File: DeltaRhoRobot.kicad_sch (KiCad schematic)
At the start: 37 parts, among them J1 Conn_01x02_Socket, J2 USB_C_Receptacle_USB2.0, J3 USB_C_Receptacle_USB2.0, Q1 MBT3904DW1, Q3 STB55NF06T4, SW1 CAS-120A1, U1 AP63205WU-7, U2 AMS1117-3.3

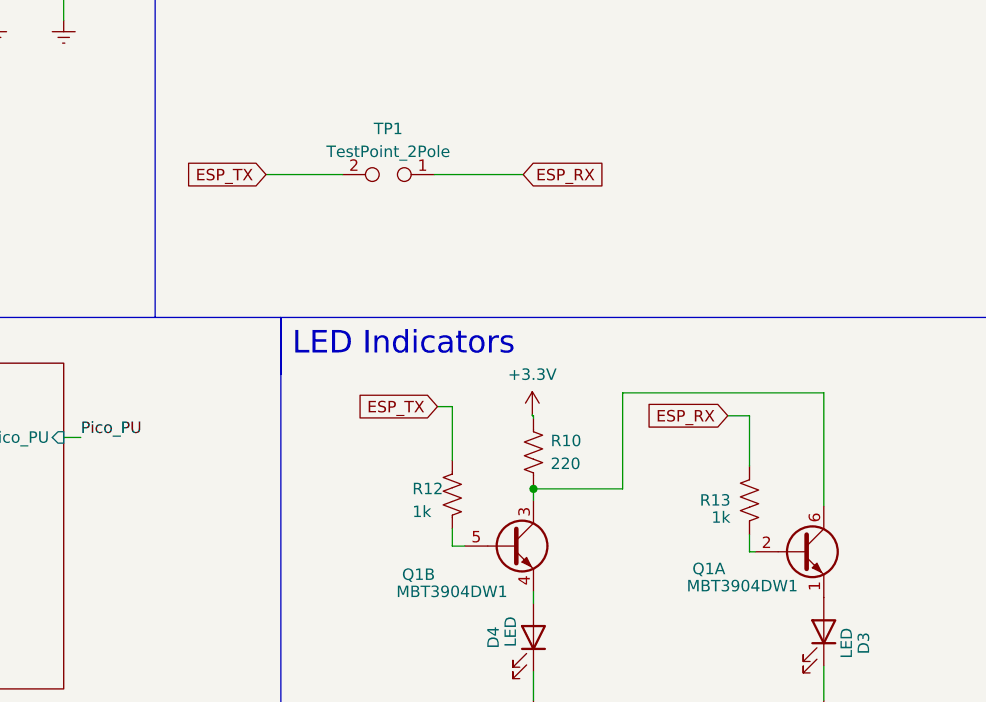
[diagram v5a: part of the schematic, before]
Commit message: update to I2C
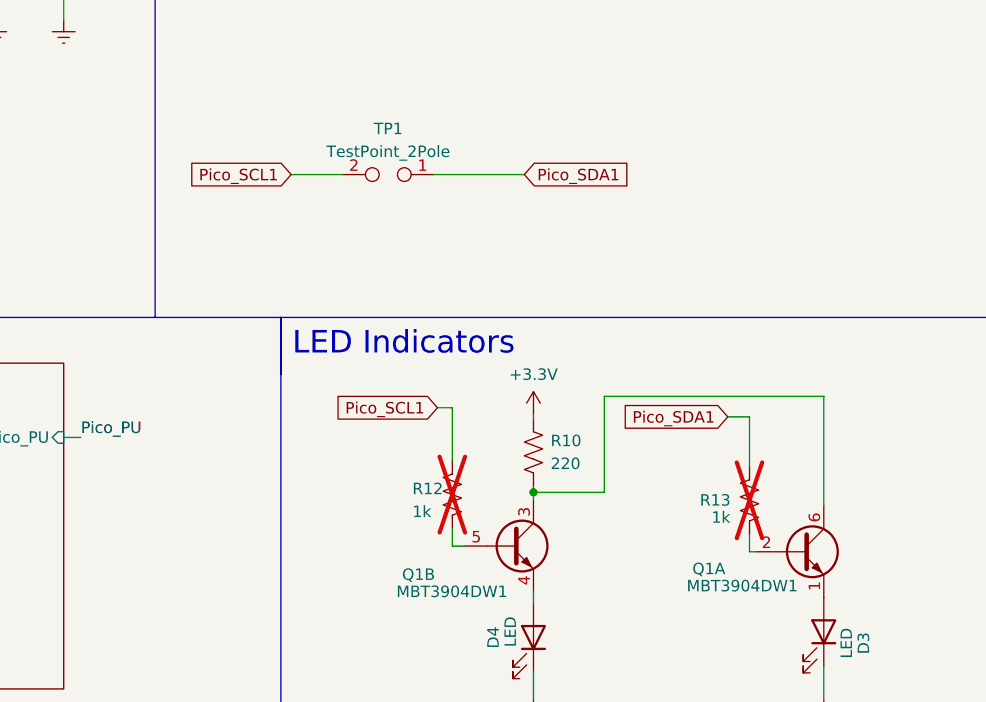
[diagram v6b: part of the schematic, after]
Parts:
- R12, R13: footprint Resistor_SMD:R_0402_1005Metric -> Resistor_SMD:R_1210_3225Metric_Pad1.30x2.65mm_HandSolder; now not fitted
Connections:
- net ESP_RX renamed Pico_SDA1
- net ESP_TX renamed Pico_SCL1
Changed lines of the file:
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@@
 (kicad_sch (version 20230121) (generator eeschema)
   (paper "A4")
+  (junction (at 124.968 170.434) (diameter 0) (color 0 0 0 0)
+  )
   (junction (at 261.366 41.783) (diameter 0) (color 0 0 0 0)
   )
@@
   )
   (junction (at 46.736 107.823) (diameter 0) (color 0 0 0 0)
-  )
-  (junction (at 124.968 170.053) (diameter 0) (color 0 0 0 0)
   )
   (no_connect (at 93.853 109.347))
@@
     (stroke (width 0) (type default))
   )
-  (wire (pts (xy 115.951 160.909) (xy 115.951 166.878))
+  (wire (pts (xy 115.951 161.036) (xy 115.951 166.878))
     (stroke (width 0) (type default))
   )
@@
     (stroke (width 0) (type default))
   )
-  (wire (pts (xy 124.841 161.925) (xy 124.841 161.798))
-    (stroke (width 0) (type default))
-  )
   (wire (pts (xy 54.991 112.903) (xy 46.736 112.903))
     (stroke (width 0) (type default))
@@
     (stroke (width 0) (type default))
   )
+  (wire (pts (xy 124.968 170.434) (xy 124.968 171.323))
+    (stroke (width 0) (type default))
+  )
   (wire (pts (xy 125.984 53.975) (xy 125.984 60.833))
     (stroke (width 0) (type default))
@@
     (stroke (width 0) (type default))
   )
+  (wire (pts (xy 124.968 169.799) (xy 124.968 170.434))
+    (stroke (width 0) (type default))
+  )
   (wire (pts (xy 236.601 51.308) (xy 254.381 51.308))
     (stroke (width 0) (type default))
@@
     (stroke (width 0) (type default))
   )
-  (wire (pts (xy 146.558 161.925) (xy 148.971 161.925))
+  (wire (pts (xy 146.558 162.052) (xy 148.971 162.052))
     (stroke (width 0) (type default))
   )
@@
     (stroke (width 0) (type default))
   )
-  (wire (pts (xy 124.968 161.925) (xy 124.841 161.925))
-    (stroke (width 0) (type default))
-  )
   (wire (pts (xy 64.516 43.053) (xy 64.516 46.228))
     (stroke (width 0) (type default))
@@
     (stroke (width 0) (type default))
   )
-  (wire (pts (xy 95.25 135.128) (xy 103.759 135.128))
+  (wire (pts (xy 98.044 135.128) (xy 103.759 135.128))
     (stroke (width 0) (type default))
   )
@@
     (stroke (width 0) (type default))
   )
-  (wire (pts (xy 124.968 169.799) (xy 124.968 170.053))
-    (stroke (width 0) (type default))
-  )
   (wire (pts (xy 48.006 39.878) (xy 58.166 39.878))
     (stroke (width 0) (type default))
@@
     (stroke (width 0) (type default))
   )
-  (wire (pts (xy 124.968 161.925) (xy 124.968 162.179))
+  (wire (pts (xy 124.968 161.798) (xy 124.968 162.179))
     (stroke (width 0) (type default))
   )
@@
     (stroke (width 0) (type default))
   )
-  (wire (pts (xy 148.971 161.925) (xy 148.971 167.513))
-    (stroke (width 0) (type default))
-  )
-  (wire (pts (xy 124.968 170.053) (xy 134.874 170.053))
+  (wire (pts (xy 148.971 162.052) (xy 148.971 167.513))
+    (stroke (width 0) (type default))
+  )
+  (wire (pts (xy 124.968 170.434) (xy 132.842 170.434))
     (stroke (width 0) (type default))
   )
@@
     (stroke (width 0) (type default))
   )
-  (wire (pts (xy 134.874 159.385) (xy 157.226 159.385))
+  (wire (pts (xy 132.842 159.766) (xy 157.226 159.766))
     (stroke (width 0) (type default))
   )
@@
     (stroke (width 0) (type default))
   )
-  (wire (pts (xy 134.874 170.053) (xy 134.874 159.385))
+  (wire (pts (xy 132.842 170.434) (xy 132.842 159.766))
     (stroke (width 0) (type default))
   )
@@
     (stroke (width 0) (type default))
   )
-  (wire (pts (xy 124.968 170.053) (xy 124.968 171.323))
-    (stroke (width 0) (type default))
-  )
-  (wire (pts (xy 114.3 160.909) (xy 115.951 160.909))
-    (stroke (width 0) (type default))
-  )
-  (wire (pts (xy 157.226 159.385) (xy 157.226 171.958))
+  (wire (pts (xy 114.3 161.036) (xy 115.951 161.036))
+    (stroke (width 0) (type default))
+  )
+  (wire (pts (xy 157.226 159.766) (xy 157.226 171.958))
     (stroke (width 0) (type default))
   )
@@
     (stroke (width 0) (type default))
   )
-  (wire (pts (xy 123.825 135.128) (xy 113.919 135.128))
+  (wire (pts (xy 113.919 135.128) (xy 123.952 135.128))
     (stroke (width 0) (type default))
   )
@@
     (effects (font (size 1.27 1.27)) (justify left bottom))
   )
-  (global_label "ESP_RX" (shape input) (at 146.558 161.925 180) (fields_autoplaced)
+  (global_label "Pico_SCL1" (shape input) (at 98.044 135.128 180) (fields_autoplaced)
     (effects (font (size 1.27 1.27)) (justify right))
-    (property "Intersheetrefs" "${INTERSHEET_REFS}" (at 136.4972 161.925 0)
+    (property "Intersheetrefs" "${INTERSHEET_REFS}" (at 85.2617 135.128 0)
       (effects (font (size 1.27 1.27)) (justify right) hide)
     )
   )
-  (global_label "ESP_TX" (shape input) (at 114.3 160.909 180) (fields_autoplaced)
+  (global_label "Pico_SDA1" (shape input) (at 123.952 135.128 0) (fields_autoplaced)
+    (effects (font (size 1.27 1.27)) (justify left))
+    (property "Intersheetrefs" "${INTERSHEET_REFS}" (at 136.7948 135.128 0)
+      (effects (font (size 1.27 1.27)) (justify left) hide)
+    )
+  )
+  (global_label "Pico_SCL1" (shape input) (at 114.3 161.036 180) (fields_autoplaced)
     (effects (font (size 1.27 1.27)) (justify right))
-    (property "Intersheetrefs" "${INTERSHEET_REFS}" (at 104.5416 160.909 0)
+    (property "Intersheetrefs" "${INTERSHEET_REFS}" (at 101.5177 161.036 0)
       (effects (font (size 1.27 1.27)) (justify right) hide)
     )
   )
-  (global_label "ESP_RX" (shape input) (at 123.825 135.128 0) (fields_autoplaced)
-    (effects (font (size 1.27 1.27)) (justify left))
-    (property "Intersheetrefs" "${INTERSHEET_REFS}" (at 133.8858 135.128 0)
-      (effects (font (size 1.27 1.27)) (justify left) hide)
-    )
-  )
-  (global_label "ESP_TX" (shape input) (at 95.25 135.128 180) (fields_autoplaced)
+  (global_label "Pico_SDA1" (shape input) (at 146.558 162.052 180) (fields_autoplaced)
     (effects (font (size 1.27 1.27)) (justify right))
-    (property "Intersheetrefs" "${INTERSHEET_REFS}" (at 85.4916 135.128 0)
+    (property "Intersheetrefs" "${INTERSHEET_REFS}" (at 133.7152 162.052 0)
       (effects (font (size 1.27 1.27)) (justify right) hide)
     )
@@
     )
   )
-  (symbol (lib_id "power:+3.3V") (at 124.841 161.798 0) (mirror y) (unit 1)
-    (in_bom yes) (on_board yes) (dnp no) (fields_autoplaced)
-    (property "Reference" "#PWR022" (at 124.841 165.608 0)
-      (effects (font (size 1.27 1.27)) hide)
-    )
-    (property "Value" "+3.3V" (at 124.841 157.353 0)
-      (effects (font (size 1.27 1.27)))
-    )
-    (property "Footprint" "" (at 124.841 161.798 0)
-      (effects (font (size 1.27 1.27)) hide)
-    )
-    (property "Datasheet" "" (at 124.841 161.798 0)
+  (symbol (lib_id "power:+3.3V") (at 124.968 161.798 0) (mirror y) (unit 1)
+    (in_bom yes) (on_board yes) (dnp no) (fields_autoplaced)
+    (property "Reference" "#PWR022" (at 124.968 165.608 0)
+      (effects (font (size 1.27 1.27)) hide)
+    )
+    (property "Value" "+3.3V" (at 124.968 157.353 0)
+      (effects (font (size 1.27 1.27)))
+    )
+    (property "Footprint" "" (at 124.968 161.798 0)
+      (effects (font (size 1.27 1.27)) hide)
+    )
+    (property "Datasheet" "" (at 124.968 161.798 0)
       (effects (font (size 1.27 1.27)) hide)
     )
@@
   )
   (symbol (lib_id "Device:R_US") (at 115.951 170.688 0) (mirror y) (unit 1)
-    (in_bom yes) (on_board yes) (dnp no)
+    (in_bom yes) (on_board yes) (dnp yes)
     (property "Reference" "R12" (at 111.506 170.053 0)
       (effects (font (size 1.27 1.27)) (justify right))
@@
       (effects (font (size 1.27 1.27)) (justify right))
     )
-    (property "Footprint" "Resistor_SMD:R_0402_1005Metric" (at 114.935 170.942 90)
+    (property "Footprint" "Resistor_SMD:R_1210_3225Metric_Pad1.30x2.65mm_HandSolder" (at 114.935 170.942 90)
       (effects (font (size 1.27 1.27)) hide)
     )
@@
   )
   (symbol (lib_id "Device:R_US") (at 148.971 171.323 0) (mirror y) (unit 1)
-    (in_bom yes) (on_board yes) (dnp no)
+    (in_bom yes) (on_board yes) (dnp yes)
     (property "Reference" "R13" (at 145.161 171.323 0)
       (effects (font (size 1.27 1.27)))
@@
       (effects (font (size 1.27 1.27)))
     )
-    (property "Footprint" "Resistor_SMD:R_0402_1005Metric" (at 147.955 171.577 90)
-      (effects (font (size 1.27 1.27)) hide)
-    )
+    (property "Footprint" "Resistor_SMD:R_1210_3225Metric_Pad1.30x2.65mm_HandSolder" (at 147.955 171.577 90)
+      (effects (font (size 1.27 1.27)) hide)
+    )

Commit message: V1.0.1
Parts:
- R4: value 10k -> 22k
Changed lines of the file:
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@@
       (effects (font (size 1.27 1.27)) (justify left))
     )
-    (property "Value" "10k" (at 191.516 107.823 0)
+    (property "Value" "22k" (at 191.516 107.823 0)
       (effects (font (size 1.27 1.27)) (justify left))
     )

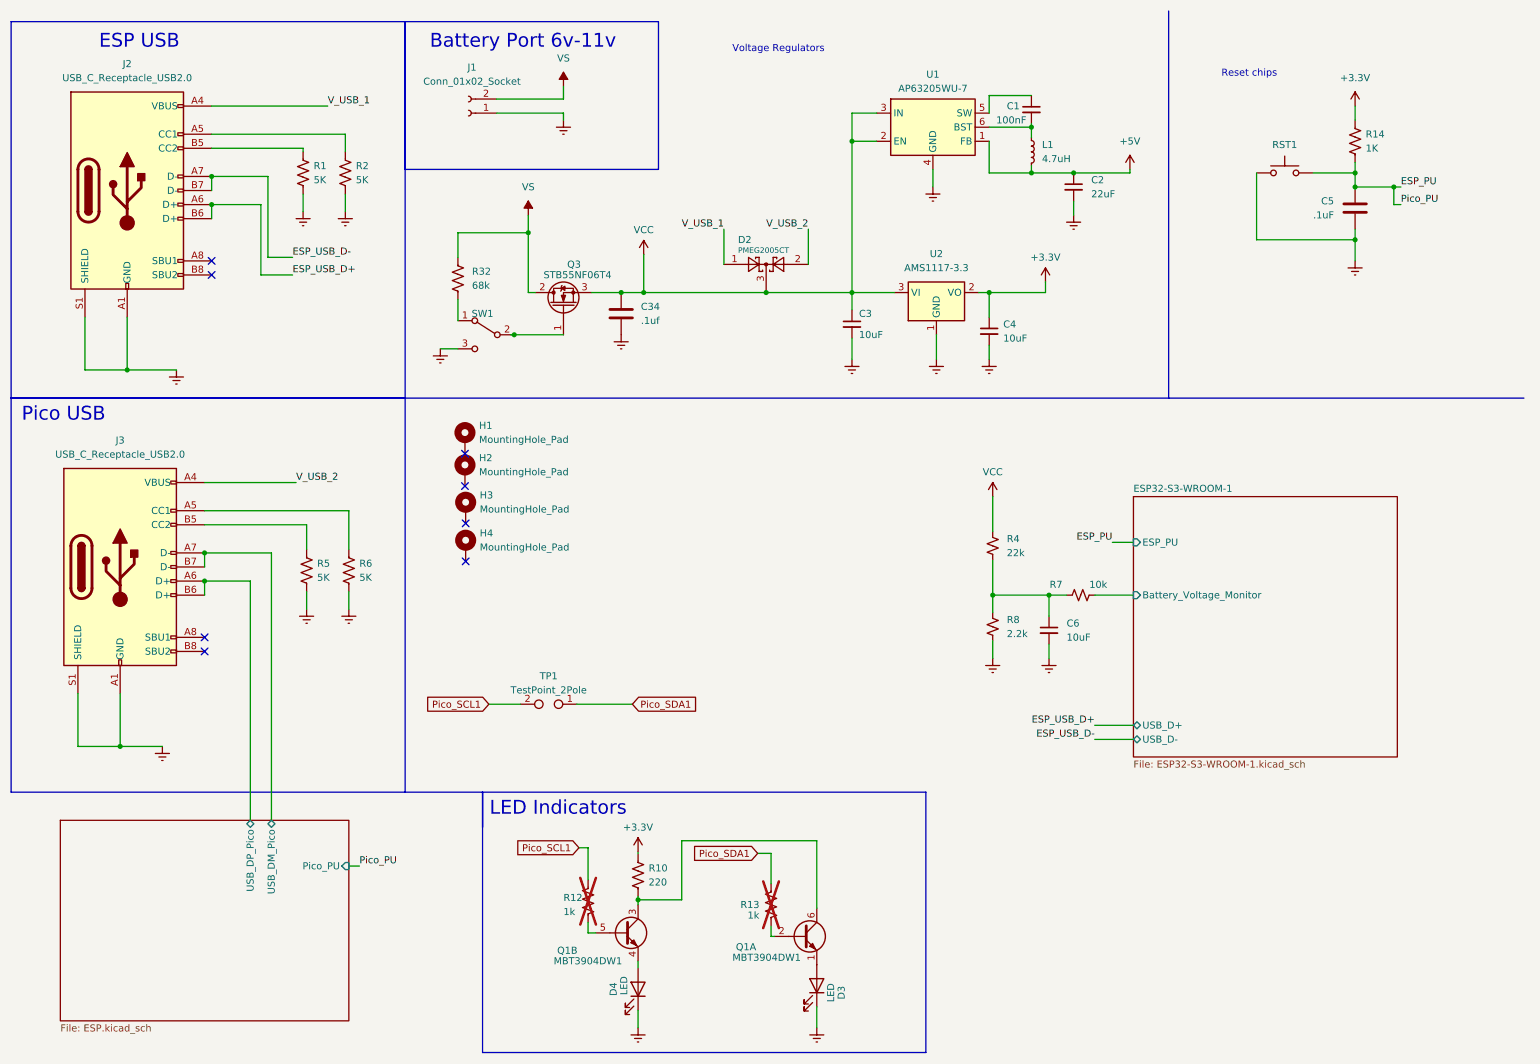
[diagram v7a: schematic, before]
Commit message: Removed 201-sized parts
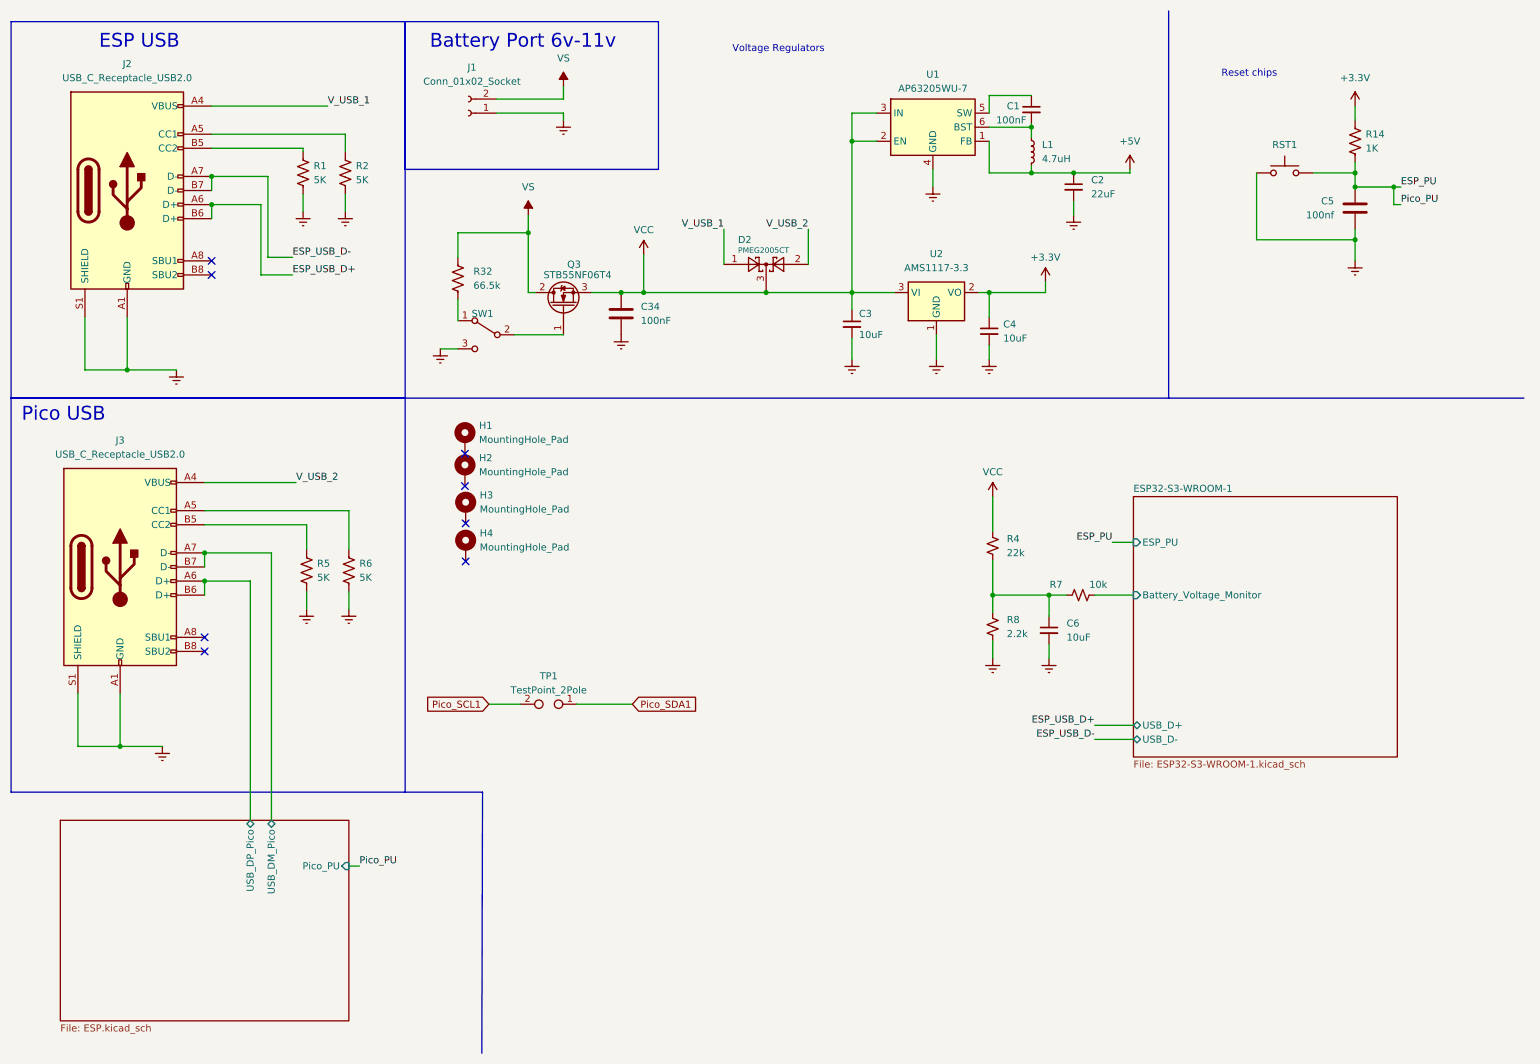
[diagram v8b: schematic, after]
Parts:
- removed D3, D4: LED, LED_SMD:LED_0402_1005Metric, symbol Device:LED
- removed Q1: MBT3904DW1, Package_TO_SOT_SMD:SOT-363_SC-70-6, symbol Transistor_BJT:MBT3904DW1
- removed R10: 220, Resistor_SMD:R_0402_1005Metric, symbol Device:R_US
- removed R12, R13: 1k, Resistor_SMD:R_1210_3225Metric_Pad1.30x2.65mm_HandSolder, symbol Device:R_US
- C1: LCSC Part # (none) -> C77020
- C2: LCSC Part # (none) -> C445459
- C3: LCSC Part # (none) -> C1713
- C34: value .1uf -> 100nF
- C4, C6: LCSC Part # (none) -> C15525
- C5: value .1uF -> 100nf; LCSC Part # (none) -> C77020
- D2: LCSC Part # (none) -> C282562
- J1: LCSC Part # (none) -> C163035
- J2, J3: footprint Connector_USB:USB_C_Receptacle_GCT_USB4105-xx-A_16P_TopMnt_Horizontal -> Connector_USB:USB_C_Receptacle_G-Switch_GT-USB-7010ASV; LCSC Part # (none) -> C2988369
- L1: LCSC Part # (none) -> C2936569
- Q3: LCSC Part # (none) -> C472532
- R1, R2, R5, R6: LCSC Part # (none) -> C477765
- R14: LCSC Part # (none) -> C279987
- R32: value 68k -> 66.5k; footprint Resistor_SMD:R_0402_1005Metric -> Resistor_SMD:R_0805_2012Metric; LCSC Part # (none) -> C101831
- R4: LCSC Part # (none) -> C82868
- R7: LCSC Part # (none) -> C60490
- R8: LCSC Part # (none) -> C25933
- RST1: LCSC Part # (none) -> C221871
- U1: LCSC Part # (none) -> C2071056
- U2: LCSC Part # (none) -> C347222
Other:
- note removed: "LED Indicators"
